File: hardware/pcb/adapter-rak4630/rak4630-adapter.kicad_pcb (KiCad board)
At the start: 2 copper layers, 53.6 x 58.4 mm, 22 parts, among them J3 USB-C, SW1 RESET, U3 USBLC6-2SC6, U4 RAK4630-8-SM-I, U5 RV-3028-C7

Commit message: Updated RAK4630 board
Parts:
- added C10: 100u 6.3V, rak4630-adapter:CPH3225A, F.Cu at (125.2, 88.9)
- added C11: 100u 6.3V, rak4630-adapter:CPH3225A, F.Cu at (121.2, 88.9)
- C7: value CPH3225A 11mF -> 100u 6.3V
- C8: value DNP -> 100u 6.3V
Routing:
- net +3V3: track 145.9 -> 125.4 mm
- net GND: track 266.7 -> 279.2 mm, vias 18 -> 20
- net IO1: track 30.8 -> 31.8 mm
- net IO5: track 51.8 -> 52.5 mm
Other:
- board text added: "Green: Booting / DFU Blue: Bluetooth"

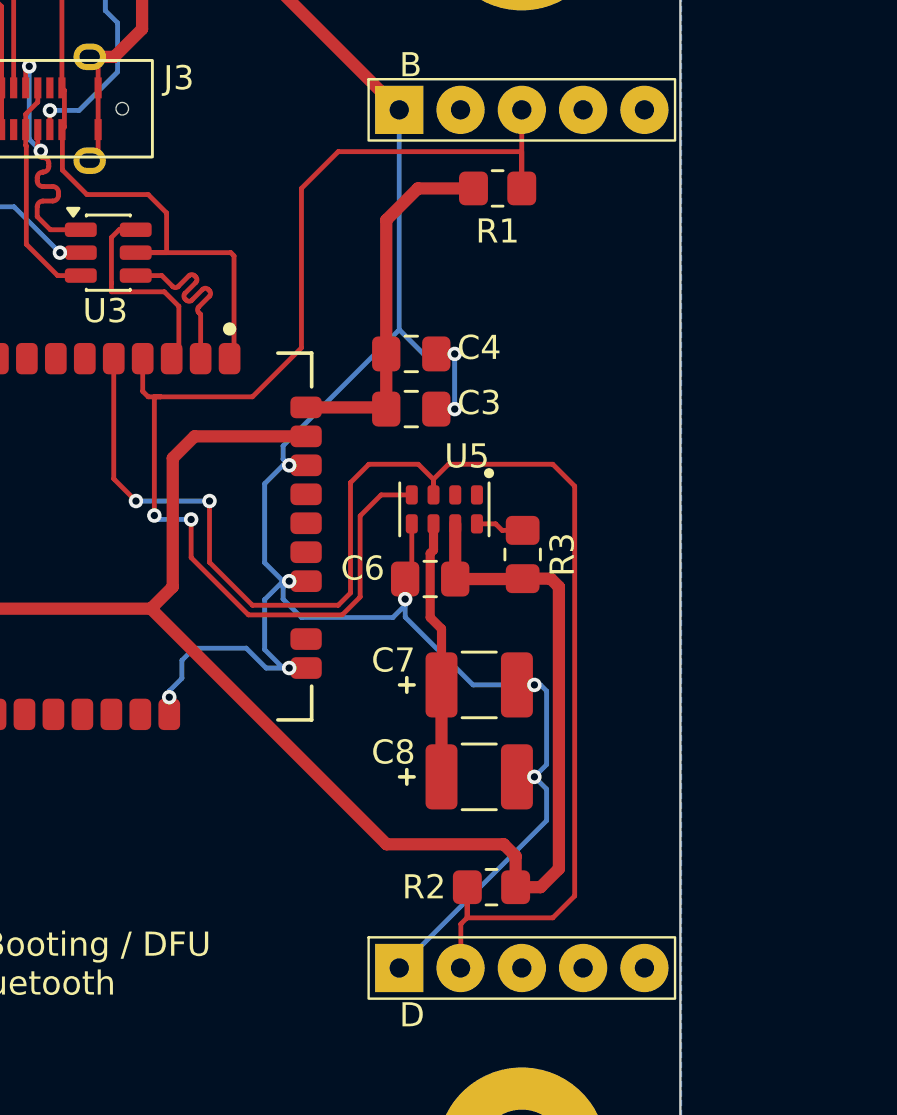
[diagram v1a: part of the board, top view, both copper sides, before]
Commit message: Updated RAK4630 adapter
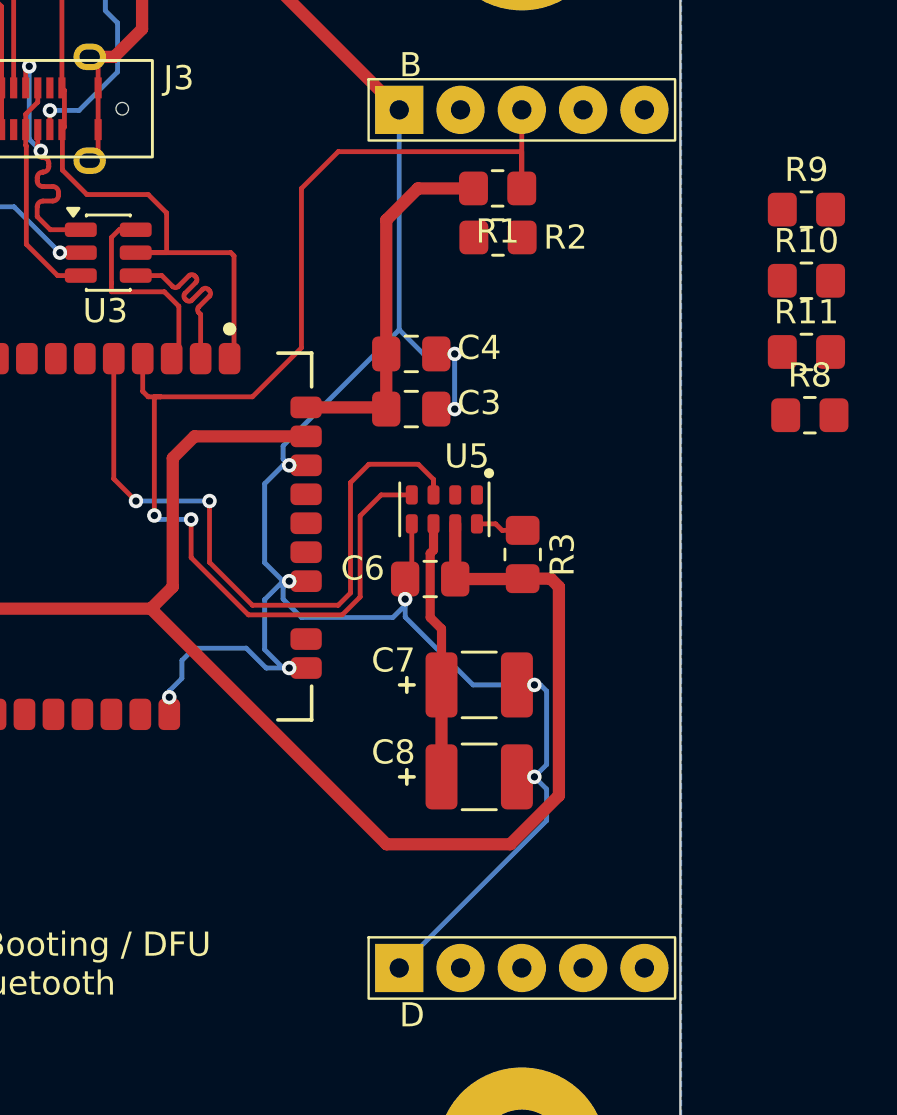
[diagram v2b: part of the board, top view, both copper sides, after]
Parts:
- added R10: 0R, Resistor_SMD:R_0805_2012Metric_Pad1.20x1.40mm_HandSolder, F.Cu at (173.8, 87.4)
- added R11: 0R, Resistor_SMD:R_0805_2012Metric_Pad1.20x1.40mm_HandSolder, F.Cu at (173.8, 90.3)
- added R8: 0R, Resistor_SMD:R_0805_2012Metric_Pad1.20x1.40mm_HandSolder, F.Cu at (174.0, 93.0)
- added R9: 0R, Resistor_SMD:R_0805_2012Metric_Pad1.20x1.40mm_HandSolder, F.Cu at (173.8, 84.4)
- R1, R2: value 10k -> 1k
- U2: value ~ -> Platform_LoRa
- moved R2 26.9 mm to (161.1, 85.6), turned to 0 degrees
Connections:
- net IO1 renamed nRESET
- net IO2 renamed SWDCLK
- net IO3 renamed SWDIO
- net IO5 renamed SDA
- R2 pad 2: IO4 -> SCL
- U2 pad 10: IO7 -> UART_TX
- U2 pad 17: IO4 -> unconnected-(U2-SCL-Pad17)
- U2 pad 7: unconnected-(U2-IO4_B-Pad7) -> SCL
- U2 pad 9: IO6 -> UART_RX
- U4 pad 10: unconnected-(U4-P0.20/UART1_TX-Pad10) -> Net-(U4-P0.20/UART1_TX)
- U4 pad 5: IO4 -> SCL
- U4 pad 6: unconnected-(U4-P0.15/UART2_RX-Pad6) -> Net-(U4-P0.15/UART2_RX)
- U4 pad 7: unconnected-(U4-P0.16/UART2_TX-Pad7) -> Net-(U4-P0.16/UART2_TX)
- U4 pad 9: unconnected-(U4-P0.19/UART1_RX-Pad9) -> Net-(U4-P0.19/UART1_RX)
- U5 pad 3: IO4 -> SCL
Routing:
- net IO4: track 61.2 -> 0.00 mm, vias 2 -> 0
- net SCL: track 0.00 -> 28.1 mm, vias 0 -> 2
- net +3V3: track 125.4 -> 121.4 mm

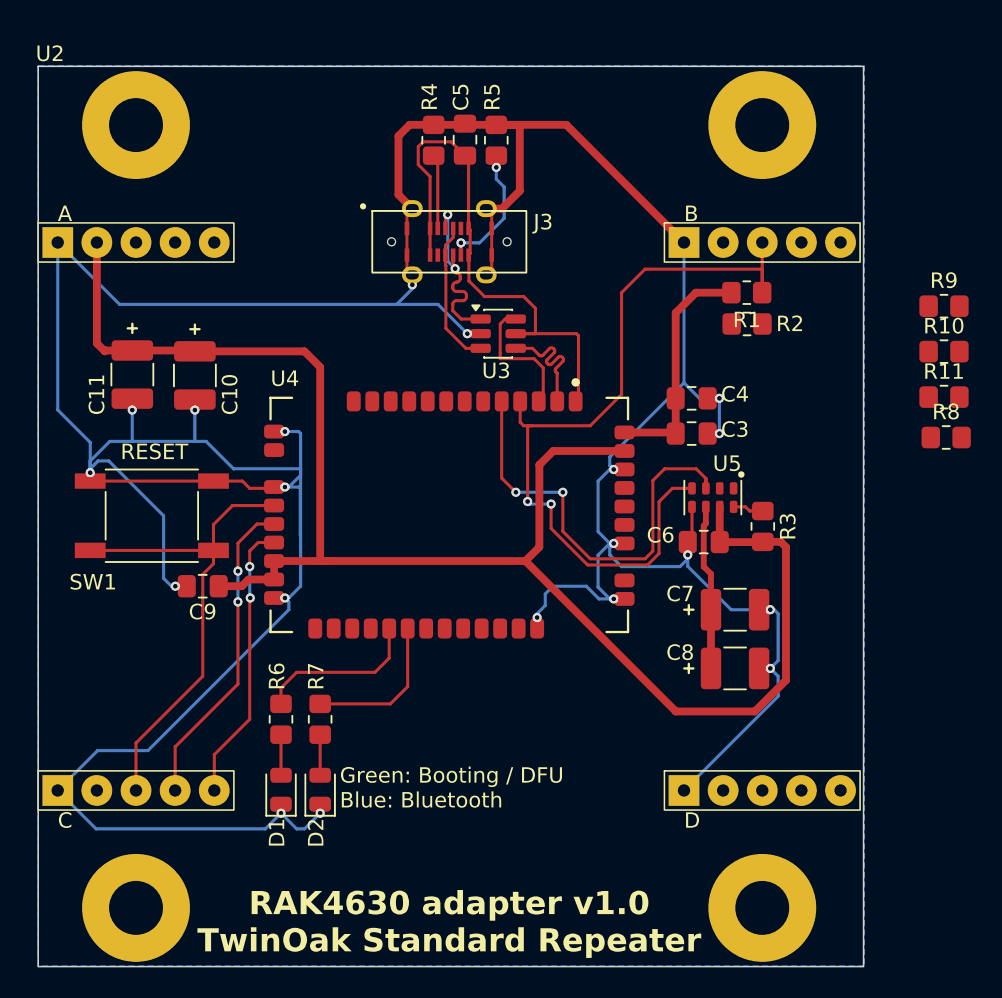
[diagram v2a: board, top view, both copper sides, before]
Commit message: Adjusted track widths on all boards
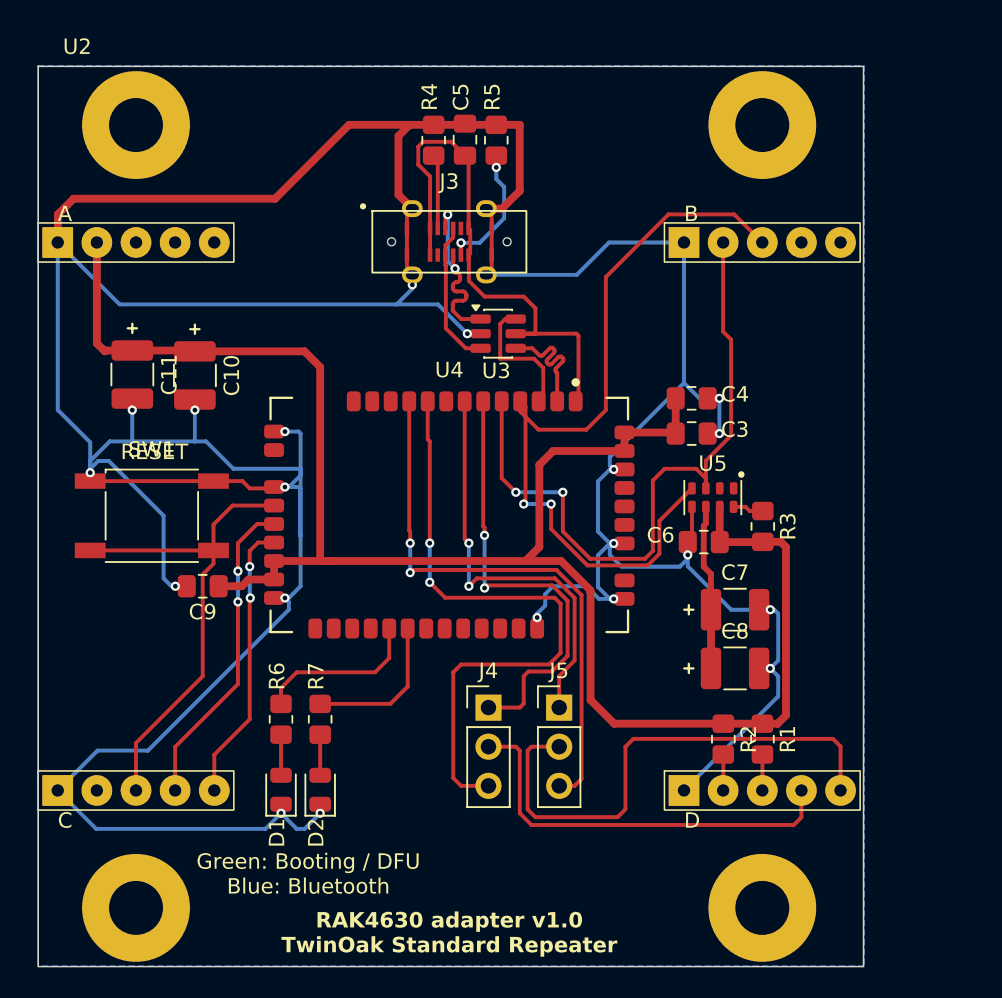
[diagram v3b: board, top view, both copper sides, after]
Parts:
- removed R10, R11, R8, R9: 0R, Resistor_SMD:R_0805_2012Metric_Pad1.20x1.40mm_HandSolder
- added J4: SER_SEL, Connector_PinHeader_2.54mm:PinHeader_1x03_P2.54mm_Vertical, F.Cu at (144.3, 110.5)
- added J5: SER_SEL, Connector_PinHeader_2.54mm:PinHeader_1x03_P2.54mm_Vertical, F.Cu at (148.9, 110.5)
- C10, C11, C7, C8: footprint rak4630-adapter:CPH3225A -> TwinOak:CPH3225A
- J3: footprint rak4630-adapter:USB_C_Receptacle_XUNPU_TYPEC-303-ACP16_Vertical -> TwinOak:USB_C_Receptacle_XUNPU_TYPEC-303-ACP16_Vertical
- SW1: footprint rak4630-adapter:SW_Push_Kinghelm_KH-6X6X5H-STM -> TwinOak:SW_Push_Kinghelm_KH-6X6X5H-STM
- U2: footprint TwinOak platform footprints:platform-adapter-footprint -> TwinOak:platform-adapter-footprint
- U4: footprint rak4630-adapter:RAK4630 -> TwinOak:RAK4630
- U5: footprint rak4630-adapter:RV-3028-C7 -> TwinOak:RV-3028-C7
- moved R1 29.0 mm to (162.1, 112.5), turned to -90 degrees
- moved R2 27.0 mm to (159.5, 112.5), turned to -90 degrees
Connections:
- R1 pad 2: SDA -> Net-(R1-Pad2)
- R2 pad 2: SCL -> Net-(R2-Pad2)
- U2 pad 10: UART_TX -> unconnected-(U2-UART_TX-Pad10)
- U2 pad 17: unconnected-(U2-SCL-Pad17) -> Net-(R2-Pad2)
- U2 pad 18: unconnected-(U2-SDA-Pad18) -> Net-(R1-Pad2)
- U2 pad 19: unconnected-(U2-UART_RX-Pad19) -> UART_RX
- U2 pad 20: unconnected-(U2-UART_TX-Pad20) -> UART_TX
- U2 pad 9: UART_RX -> unconnected-(U2-UART_RX-Pad9)
- U4 pad 10: Net-(U4-P0.20/UART1_TX) -> SER2_TX
- U4 pad 6: Net-(U4-P0.15/UART2_RX) -> SER1_RX
- U4 pad 7: Net-(U4-P0.16/UART2_TX) -> SER1_TX
- U4 pad 9: Net-(U4-P0.19/UART1_RX) -> SER2_RX
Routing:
- net SER2_RX: track 0.00 -> 40.9 mm, vias 0 -> 2
- net SER2_TX: track 0.00 -> 36.6 mm, vias 0 -> 2
- net UART_TX: track 0.00 -> 34.0 mm
- net SER1_RX: track 0.00 -> 29.2 mm, vias 0 -> 2
- net SER1_TX: track 0.00 -> 27.2 mm, vias 0 -> 2
- net UART_RX: track 0.00 -> 26.7 mm
- net GND: track 279.2 -> 304.7 mm
- net SCL: track 28.1 -> 45.0 mm
- net +3V3: track 121.4 -> 119.0 mm
- net Net-(R2-Pad2): track 0.00 -> 2.34 mm
- net Net-(R1-Pad2): track 0.00 -> 2.34 mm

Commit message: Cleanup of schematics and pcb traces on RAK4630 adapter
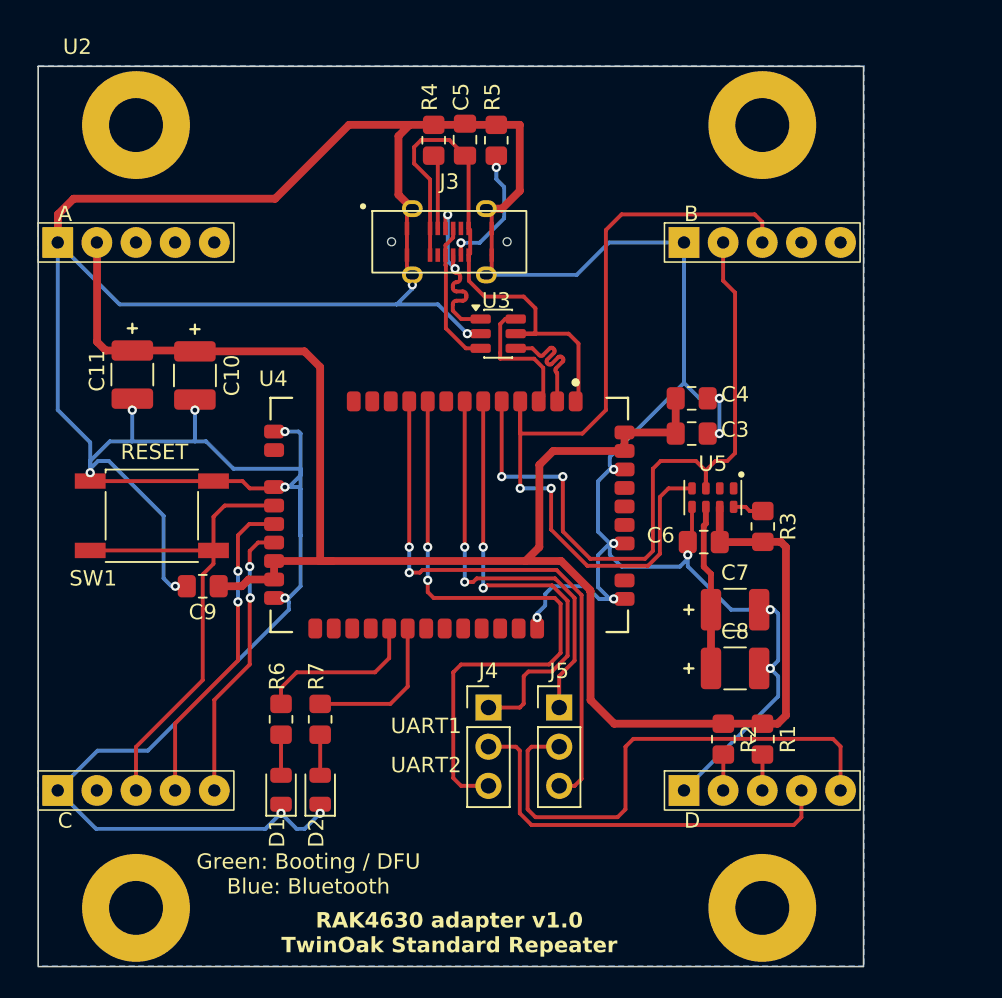
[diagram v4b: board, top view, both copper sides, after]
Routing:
- net SDA: track 52.1 -> 56.8 mm
- net SCL: track 45.0 -> 47.5 mm
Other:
- board text added: "UART1"
- board text added: "UART2"

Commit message: Misc changes
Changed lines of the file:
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@@
 		(layer "F.Cu")
 		(at 158.83 96.866)
-		(descr "Micro Crystal RV-3028-C7 RTC, C7 ceramic SMD 3.2x1.5x0.8mm, 8 pads. Land pattern per Micro Crystal C7 app manual (pads 0.5x0.8, pitch 0.9, rows 1.2mm c2c). Pin 1 top-right. Lid = VSS.")
+		(descr "Micro Crystal RV-3028-C7 RTC, C7 ceramic SMD 3.2x1.5x0.8mm, 8 pads. Land pattern per Micro Crystal C7 app manual (pads 0.5x0.8, pitch 0.9, rows 1.2mm c2c). Pin 1 top-left (pad numbering corrected 2026-08-11 — was mirrored). Lid = VSS.")
 		(tags "RTC RV-3028 Micro Crystal C7")
 		(property "Reference" "U5"
@@
 		)
 		(fp_circle
-			(center 1.85 -1.5)
-			(end 2 -1.5)
+			(center -1.85 -1.5)
+			(end -2 -1.5)
 			(stroke
 				(width 0.12)
@@
 		)
 		(fp_line
-			(start 1.1 -0.75)
-			(end 1.6 -0.25)
+			(start -1.1 -0.75)
+			(end -1.6 -0.25)
 			(stroke
 				(width 0.1)
@@
 		)
 		(pad "1" smd roundrect
-			(at 1.35 -0.6)
+			(at -1.35 -0.6)
 			(size 0.5 0.8)
 			(layers "F.Cu" "F.Mask" "F.Paste")
@@
 		)
 		(pad "2" smd roundrect
-			(at 0.45 -0.6)
+			(at -0.45 -0.6)
 			(size 0.5 0.8)
 			(layers "F.Cu" "F.Mask" "F.Paste")
@@
 		)
 		(pad "3" smd roundrect
-			(at -0.45 -0.6)
+			(at 0.45 -0.6)
 			(size 0.5 0.8)
 			(layers "F.Cu" "F.Mask" "F.Paste")
@@
 		)
 		(pad "4" smd roundrect
-			(at -1.35 -0.6)
+			(at 1.35 -0.6)
 			(size 0.5 0.8)
 			(layers "F.Cu" "F.Mask" "F.Paste")
@@
 		)
 		(pad "5" smd roundrect
-			(at -1.35 0.6)
+			(at 1.35 0.6)
 			(size 0.5 0.8)
 			(layers "F.Cu" "F.Mask" "F.Paste")
@@
 		)
 		(pad "6" smd roundrect
-			(at -0.45 0.6)
+			(at 0.45 0.6)
 			(size 0.5 0.8)
 			(layers "F.Cu" "F.Mask" "F.Paste")
@@
 		)
 		(pad "7" smd roundrect
-			(at 0.45 0.6)
+			(at -0.45 0.6)
 			(size 0.5 0.8)
 			(layers "F.Cu" "F.Mask" "F.Paste")
@@
 		)
 		(pad "8" smd roundrect
-			(at 1.35 0.6)
-			(size 0.5 0.8)
-			(layers "F.Cu" "F.Mask" "F.Paste")
+			(at -1.35 0.6)
+			(size 0.5 0.8)
+			(layers "F.Cu" "F.Mask" "F.Paste")

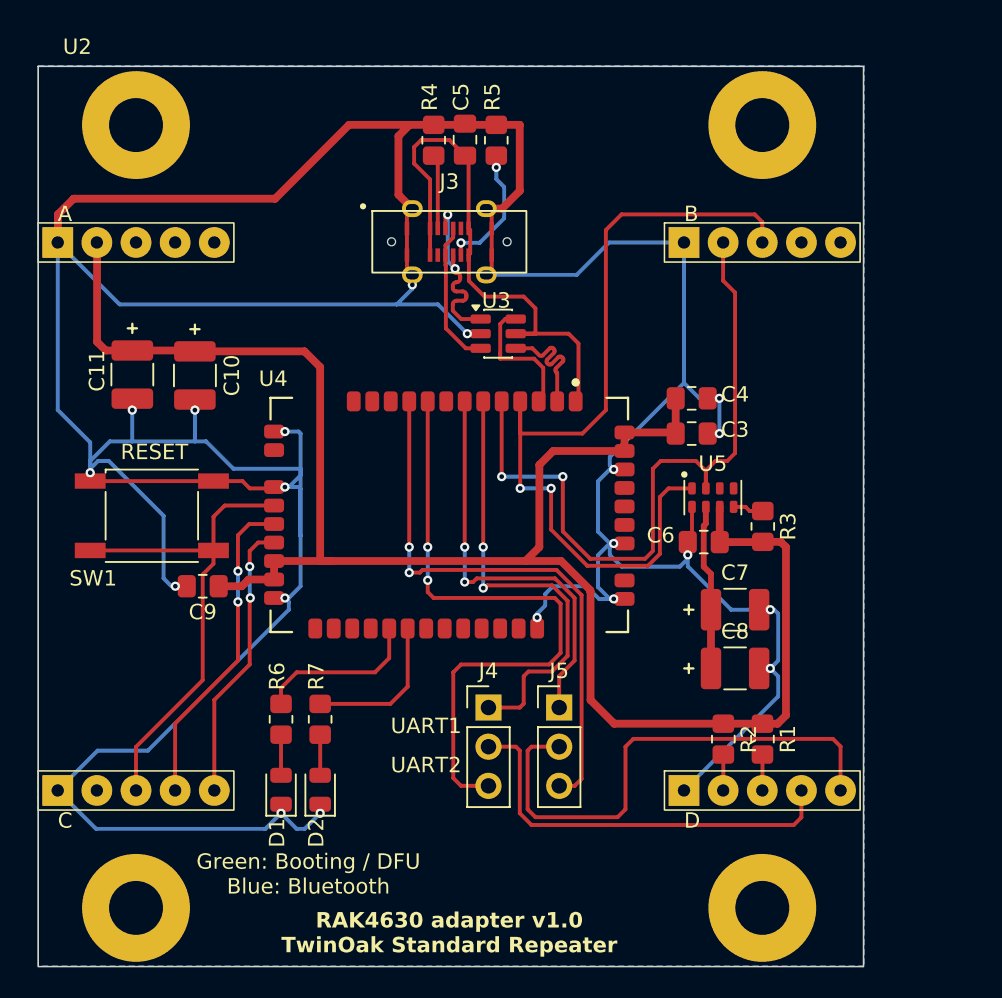
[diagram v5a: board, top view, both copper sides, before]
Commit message: Updates according to preflight
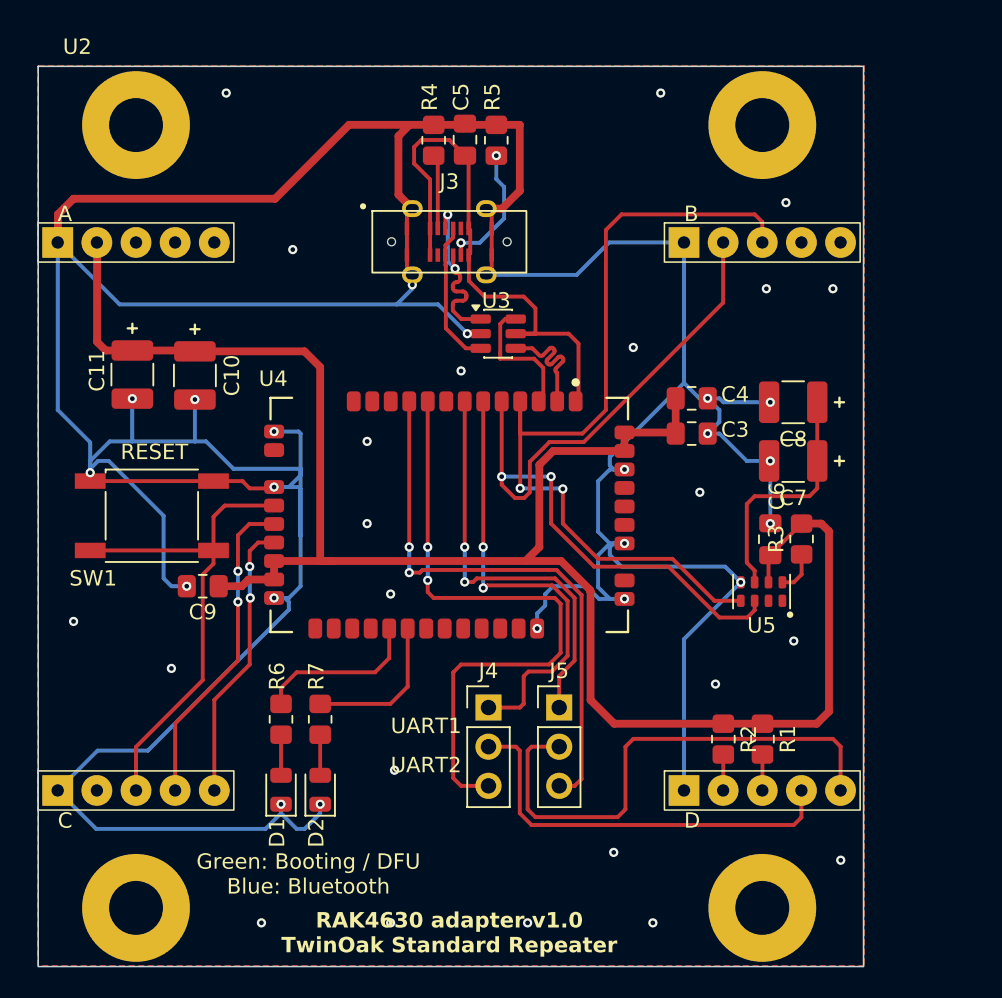
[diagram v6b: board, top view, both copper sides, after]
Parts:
- moved C8 17.7 mm to (164.0, 90.7), turned to 180 degrees
- moved C7 10.4 mm to (164.0, 94.5), turned to 180 degrees
- moved U5 6.87 mm to (162.0, 103.0), turned to 180 degrees
- moved C6 4.32 mm to (162.6, 99.6), turned to 90 degrees
- moved R3 2.65 mm to (164.6, 99.6), turned to 90 degrees
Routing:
- net SCL: track 47.5 -> 53.4 mm
- net GND: track 304.7 -> 310.5 mm, vias 20 -> 44
- net Net-(U5-VBACKUP): track 10.7 -> 15.9 mm
- net +3V3: track 118.9 -> 122.5 mm
- net Net-(U5-EVI): track 2.01 -> 2.76 mm
- added copper zone on F.Cu, net GND
